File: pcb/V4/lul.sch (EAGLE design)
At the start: 90 parts, among them IC1 STM32F072C8T6, IC2 REG1117, IC3 74AHCT1G08DBV, SW1 324_SW324_SWITCH_FOOT_HOLE, SW10 KAILH_SWITCH_SOCKET, SW11 KAILH_SWITCH_SOCKET, SW12 KAILH_SWITCH_SOCKET, SW13 KAILH_SWITCH_SOCKET, SW14 KAILH_SWITCH_SOCKET, SW15 KAILH_SWITCH_SOCKET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

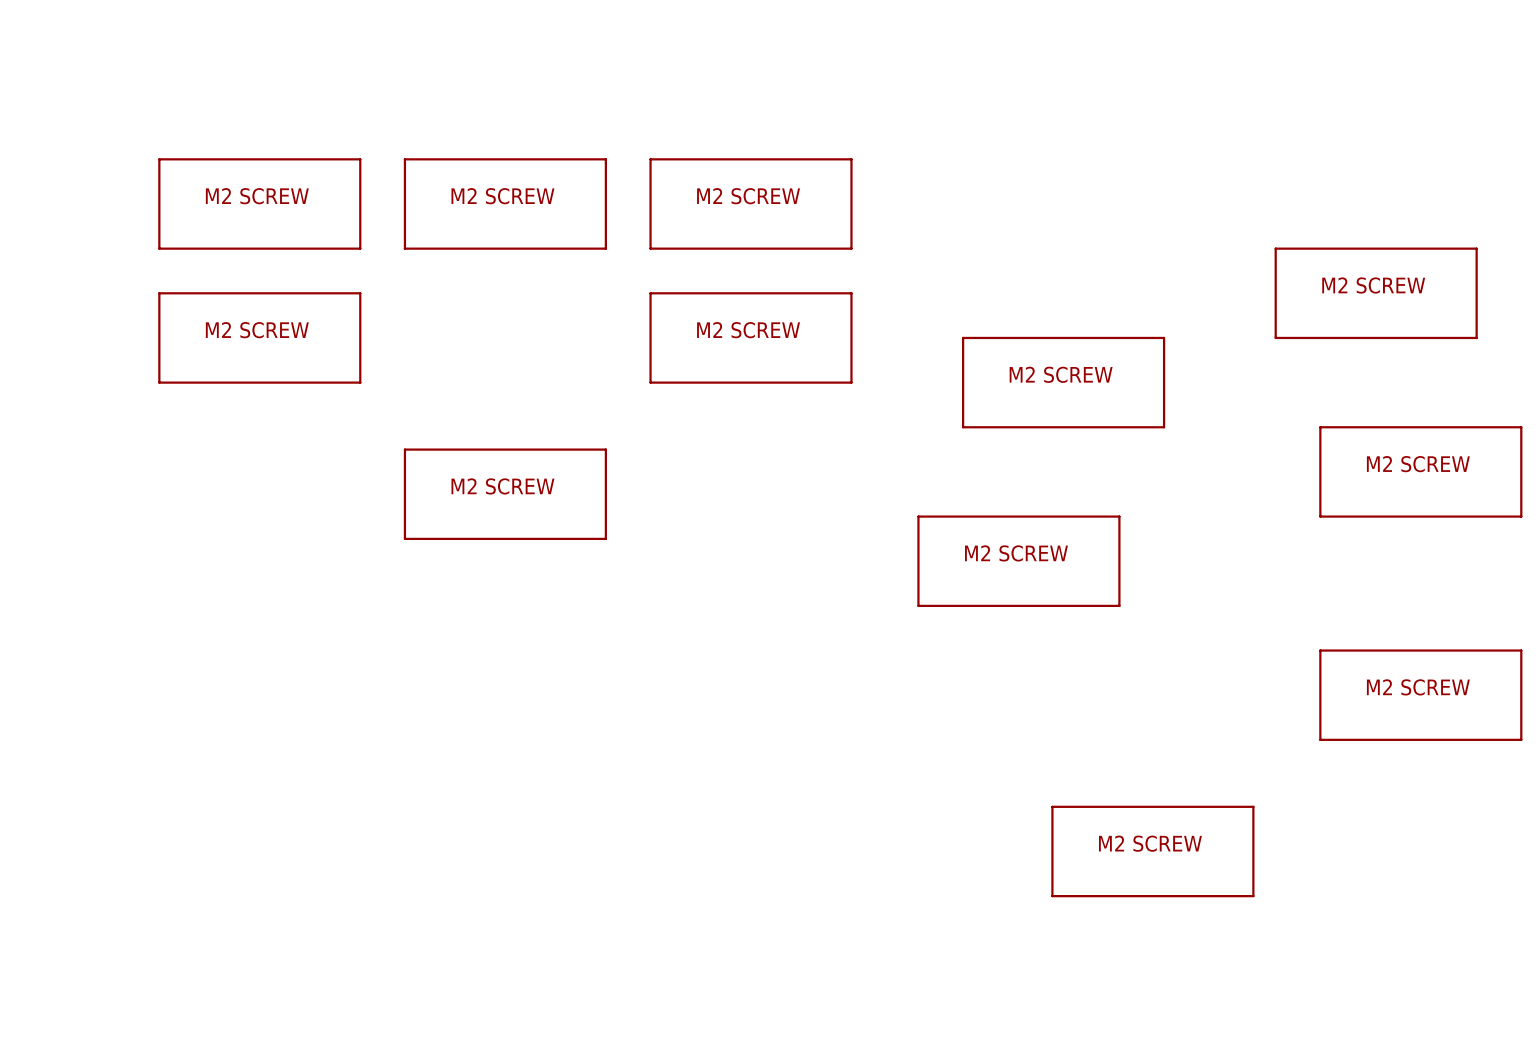
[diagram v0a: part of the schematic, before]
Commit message: modified mounting plate design
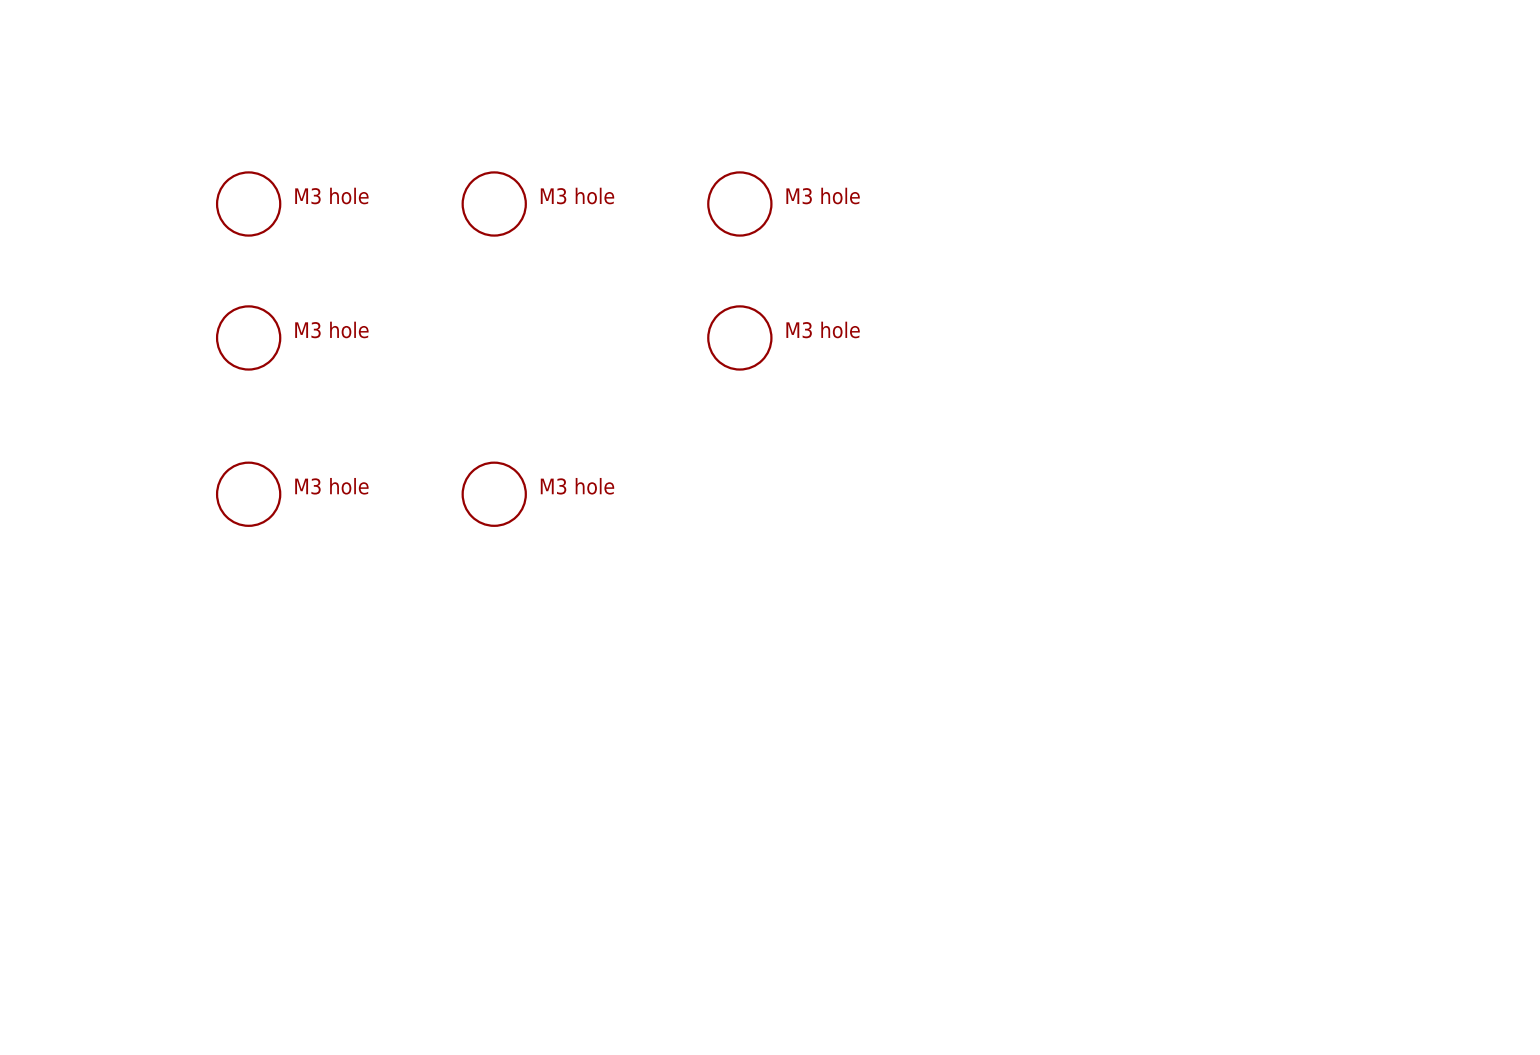
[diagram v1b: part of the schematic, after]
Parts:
- removed U$12, U$13, U$17, U$22, U$23, U$8: M2_SCREW_DEV, 3pos_slide_switch_centered:M2_SCREW_DEV
- added U$14: M3_MOUNTING_HOLE, clock:M3_MOUNTING_HOLE
- U$10, U$11, U$15, U$16, U$7, U$9: value M2_SCREW_DEV -> M3_MOUNTING_HOLE; device 3pos_slide_switch_centered:M2_SCREW_DEV -> clock:M3_MOUNTING_HOLE
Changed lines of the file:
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@@
 <part name="+3V32" library="supply1" library_urn="urn:adsk.eagle:library:371" deviceset="+3V3" device=""/>
 <part name="C27" library="clock" deviceset="C-US" device="C1210" value="47uF"/>
-<part name="U$7" library="3pos_slide_switch_centered" deviceset="M2_SCREW_DEV" device=""/>
-<part name="U$9" library="3pos_slide_switch_centered" deviceset="M2_SCREW_DEV" device=""/>
-<part name="U$10" library="3pos_slide_switch_centered" deviceset="M2_SCREW_DEV" device=""/>
-<part name="U$11" library="3pos_slide_switch_centered" deviceset="M2_SCREW_DEV" device=""/>
-<part name="U$15" library="3pos_slide_switch_centered" deviceset="M2_SCREW_DEV" device=""/>
-<part name="U$16" library="3pos_slide_switch_centered" deviceset="M2_SCREW_DEV" device=""/>
+<part name="U$7" library="clock" deviceset="M3_MOUNTING_HOLE" device=""/>
+<part name="U$9" library="clock" deviceset="M3_MOUNTING_HOLE" device=""/>
+<part name="U$10" library="clock" deviceset="M3_MOUNTING_HOLE" device=""/>
+<part name="U$11" library="clock" deviceset="M3_MOUNTING_HOLE" device=""/>
+<part name="U$14" library="clock" deviceset="M3_MOUNTING_HOLE" device=""/>
+<part name="U$15" library="clock" deviceset="M3_MOUNTING_HOLE" device=""/>
+<part name="U$16" library="clock" deviceset="M3_MOUNTING_HOLE" device=""/>
 <part name="R7" library="clock" deviceset="RESISTOR" device="0805-RES" value="5.1K"/>
 <part name="R8" library="clock" deviceset="RESISTOR" device="0805-RES" value="5.1K"/>
@@
 <part name="SW18" library="Kailh_switch_socket" deviceset="KAILH_SWITCH_SOCKET" device=""/>
 <part name="SW19" library="Kailh_switch_socket" deviceset="KAILH_SWITCH_SOCKET" device=""/>
-<part name="U$8" library="3pos_slide_switch_centered" deviceset="M2_SCREW_DEV" device=""/>
-<part name="U$12" library="3pos_slide_switch_centered" deviceset="M2_SCREW_DEV" device=""/>
-<part name="U$13" library="3pos_slide_switch_centered" deviceset="M2_SCREW_DEV" device=""/>
-<part name="U$17" library="3pos_slide_switch_centered" deviceset="M2_SCREW_DEV" device=""/>
-<part name="U$22" library="3pos_slide_switch_centered" deviceset="M2_SCREW_DEV" device=""/>
-<part name="U$23" library="3pos_slide_switch_centered" deviceset="M2_SCREW_DEV" device=""/>
 </parts>
 <sheets>
@@
 <instance part="U$10" gate="G$1" x="467.36" y="33.02" smashed="yes"/>
 <instance part="U$11" gate="G$1" x="523.24" y="33.02" smashed="yes"/>
+<instance part="U$14" gate="G$1" x="467.36" y="15.24" smashed="yes"/>
 <instance part="U$15" gate="G$1" x="495.3" y="48.26" smashed="yes"/>
 <instance part="U$16" gate="G$1" x="523.24" y="48.26" smashed="yes"/>
@@
 <attribute name="VALUE" x="172.72" y="-48.26" size="1.778" layer="96"/>
 </instance>
-<instance part="U$8" gate="G$1" x="594.36" y="38.1" smashed="yes"/>
-<instance part="U$12" gate="G$1" x="599.44" y="17.78" smashed="yes"/>
-<instance part="U$13" gate="G$1" x="599.44" y="-7.62" smashed="yes"/>
-<instance part="U$17" gate="G$1" x="568.96" y="-25.4" smashed="yes"/>
-<instance part="U$22" gate="G$1" x="553.72" y="7.62" smashed="yes"/>
-<instance part="U$23" gate="G$1" x="558.8" y="27.94" smashed="yes"/>
 </instances>
 <busses>
